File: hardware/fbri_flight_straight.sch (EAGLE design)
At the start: 38 parts, among them U1 SAM_D20E, U2 SI4060, U3 MAX1947, U4 ANTENOVA_GPS_M10382, U5 S25FS-S

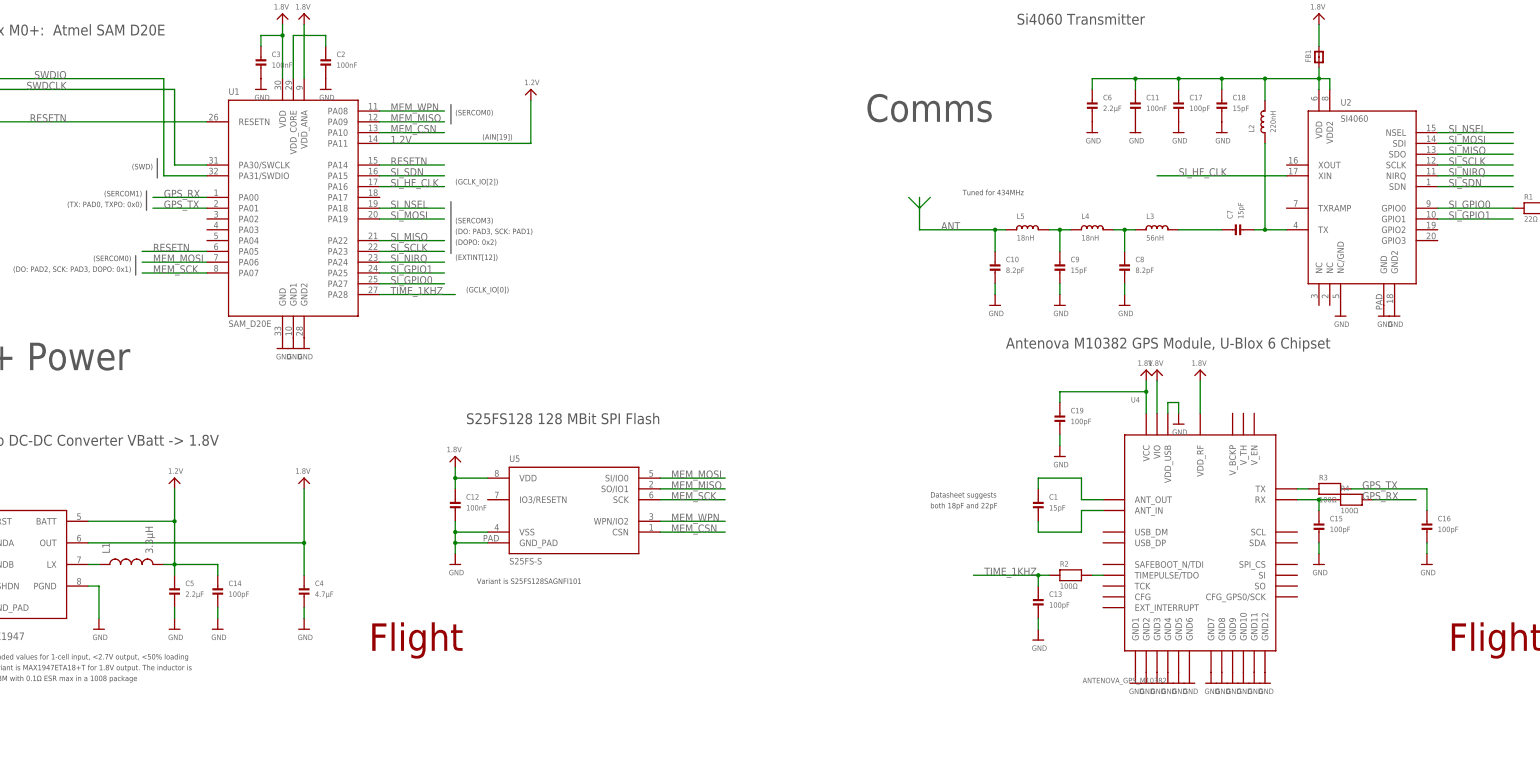
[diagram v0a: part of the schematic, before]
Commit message: Nearly there, about to re-work MAX1947
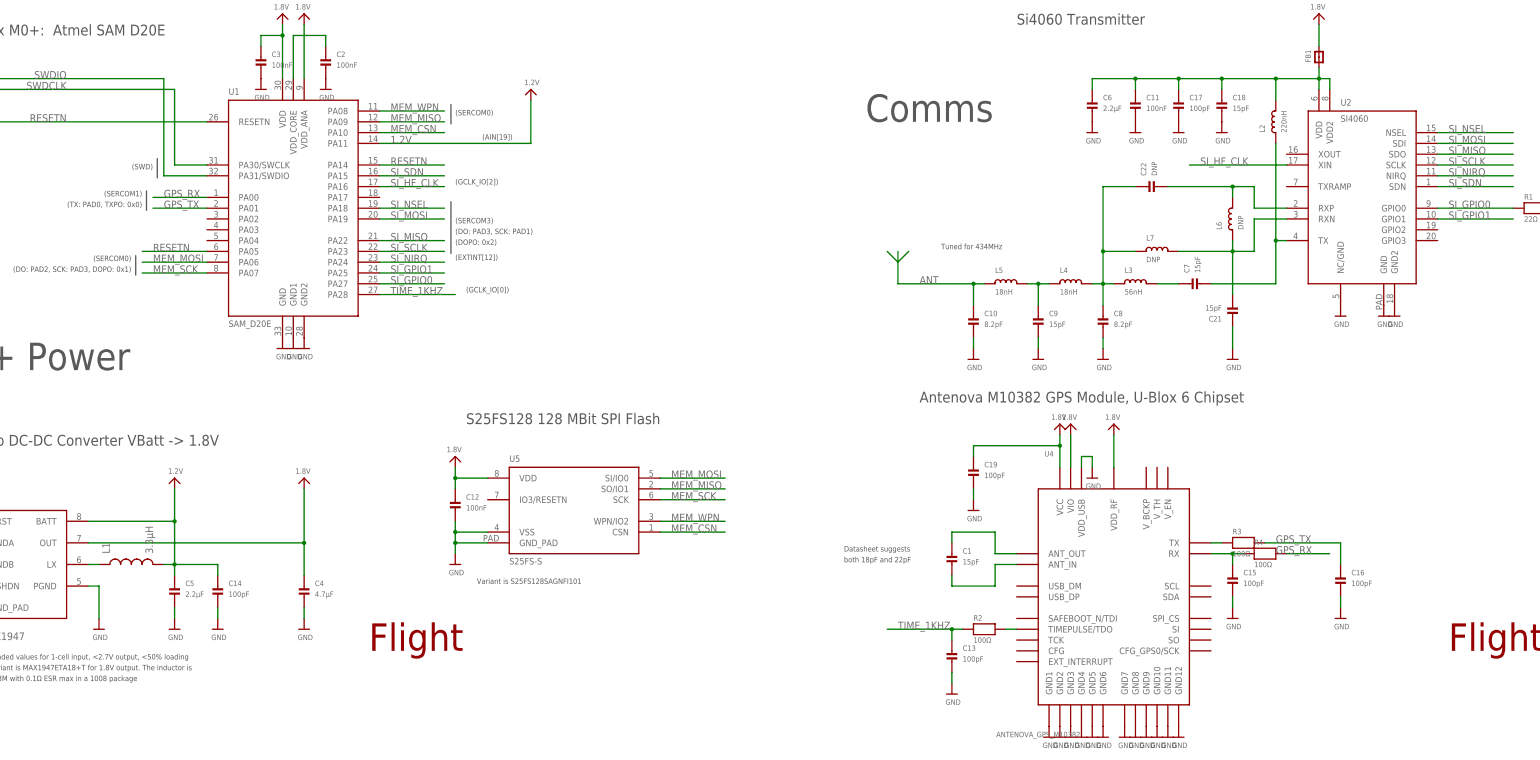
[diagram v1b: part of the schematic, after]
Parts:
- added C21: 15pF, microbuilder_v3:CAP_CERAMIC_0402
- added C22: DNP, microbuilder_v3:CAP_CERAMIC_0402
- added L6, L7: DNP, microbuilder_v3:INDUCTOR_0402
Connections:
- new net RXN: C21.P$2, L6.1, L7.2, U2.RXN
- new net RXP: C22.P$2, L6.2, U2.RXP
- net FILTER1: now also C22.P$1, L7.1
- net GND: now also C21.P$1
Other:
- moved on the sheet: C1, C10, C13, C15, C16, C19, C7, C8, C9, L2, L3, L4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

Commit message: Before rename
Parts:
- removed C4: 4.7µF, microbuilder_v3:CAP_CERAMIC_0402
- added C23: 4.7µF, resistor:C-EUC0603K
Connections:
- net 1.8V: now also C23.1; no longer C4.P$1
- net GND: now also C23.2; no longer C4.P$2
- net RESETN: now also U1.PA15; no longer U1.PA14
- net SI_HF_CLK: now also U1.PA17; no longer U1.PA16
- net SI_SDN: now also U1.PA16; no longer U1.PA15
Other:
- note added: "(GCLK_IO[3])"
- note removed: "(GCLK_IO[2])"
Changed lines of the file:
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@@
 <part name="U$1" library="microbuilder_v3" deviceset="GND" device=""/>
 <part name="U$28" library="microbuilder_v3" deviceset="GND" device=""/>
-<part name="C4" library="microbuilder_v3" deviceset="CAP_CERAMIC" device="_0402" value="4.7µF"/>
 <part name="U$29" library="microbuilder_v3" deviceset="GND" device=""/>
 <part name="U$30" library="microbuilder_v3" deviceset="1.8V" device=""/>
@@
 <part name="L7" library="microbuilder_v3" deviceset="INDUCTOR" device="_0402" value="DNP"/>
 <part name="C22" library="microbuilder_v3" deviceset="CAP_CERAMIC" device="_0402" value="DNP"/>
+<part name="C23" library="resistor" deviceset="C-EU" device="C0603K" value="4.7µF"/>
 </parts>
 <sheets>
@@
 <wire x1="169.164" y1="153.924" x2="169.164" y2="149.352" width="0.1524" layer="97"/>
 <text x="93.98" y="114.554" size="1.27" layer="97" font="vector" ratio="11" rot="MR0">(DO: PAD2, SCK: PAD3, DOPO: 0x1)</text>
-<text x="170.18" y="135.128" size="1.27" layer="97" font="vector" ratio="11">(GCLK_IO[2])</text>
+<text x="170.18" y="132.588" size="1.27" layer="97" font="vector" ratio="11">(GCLK_IO[3])</text>
 <text x="96.52" y="132.334" size="1.27" layer="97" font="vector" ratio="11" rot="MR0">(SERCOM1)</text>
 <wire x1="97.536" y1="133.604" x2="97.536" y2="129.032" width="0.1524" layer="97"/>
@@
 <instance part="U$1" gate="G$1" x="50.8" y="30.48"/>
 <instance part="U$28" gate="G$1" x="86.36" y="30.48"/>
-<instance part="C4" gate="G$1" x="134.62" y="38.1"/>
 <instance part="U$29" gate="G$1" x="134.62" y="30.48"/>
 <instance part="U$30" gate="G$1" x="134.62" y="66.04" rot="MR0"/>
@@
 <instance part="L7" gate="G$1" x="335.28" y="119.38"/>
 <instance part="C22" gate="G$1" x="335.28" y="134.62" rot="R90"/>
+<instance part="C23" gate="G$1" x="134.62" y="43.18"/>
 </instances>
 <busses>
@@
 <segment>
 <pinref part="U$29" gate="G$1" pin="GND"/>
-<pinref part="C4" gate="G$1" pin="P$2"/>
-<wire x1="134.62" y1="33.02" x2="134.62" y2="35.56" width="0.1524" layer="91"/>
+<pinref part="C23" gate="G$1" pin="2"/>
+<wire x1="134.62" y1="33.02" x2="134.62" y2="38.1" width="0.1524" layer="91"/>
 </segment>
 <segment>
@@
 </segment>
 <segment>
-<pinref part="U1" gate="G$1" pin="PA14"/>
-<wire x1="152.4" y1="139.7" x2="167.64" y2="139.7" width="0.1524" layer="91"/>
-<label x="154.94" y="139.7" size="1.778" layer="95" ratio="11"/>
+<pinref part="U1" gate="G$1" pin="PA15"/>
+<wire x1="152.4" y1="137.16" x2="167.64" y2="137.16" width="0.1524" layer="91"/>
+<label x="154.94" y="137.16" size="1.778" layer="95"/>
 </segment>
 </net>
@@
 <segment>
 <pinref part="U3" gate="G$1" pin="OUT"/>
-<pinref part="C4" gate="G$1" pin="P$1"/>
 <wire x1="83.82" y1="50.8" x2="134.62" y2="50.8" width="0.1524" layer="91"/>
-<wire x1="134.62" y1="50.8" x2="134.62" y2="43.18" width="0.1524" layer="91"/>
 <pinref part="U$30" gate="G$1" pin="1.8V"/>
 <wire x1="134.62" y1="50.8" x2="134.62" y2="63.5" width="0.1524" layer="91"/>
 <junction x="134.62" y="50.8"/>
+<pinref part="C23" gate="G$1" pin="1"/>
+<wire x1="134.62" y1="50.8" x2="134.62" y2="45.72" width="0.1524" layer="91"/>
 </segment>
 <segment>
@@
 </segment>
 <segment>
-<pinref part="U1" gate="G$1" pin="PA16"/>
-<wire x1="152.4" y1="134.62" x2="167.64" y2="134.62" width="0.1524" layer="91"/>
-<label x="154.94" y="134.62" size="1.778" layer="95" ratio="11"/>
+<pinref part="U1" gate="G$1" pin="PA17"/>
+<wire x1="152.4" y1="132.08" x2="167.64" y2="132.08" width="0.1524" layer="91"/>
+<label x="154.94" y="132.08" size="1.778" layer="95"/>
 </segment>
 </net>
 <net name="SI_SDN" class="0">
-<segment>
-<pinref part="U1" gate="G$1" pin="PA15"/>
-<wire x1="152.4" y1="137.16" x2="167.64" y2="137.16" width="0.1524" layer="91"/>
-<label x="154.94" y="137.16" size="1.778" layer="95" ratio="11"/>
-</segment>
 <segment>
 <pinref part="U2" gate="G$1" pin="SDN"/>
@@
 <label x="403.86" y="134.62" size="1.778" layer="95" ratio="11"/>
 </segment>
-</net>
+<segment>
+<pinref part="U1" gate="G$1" pin="PA16"/>
+<wire x1="152.4" y1="134.62" x2="167.64" y2="134.62" width="0.1524" layer="91"/>
+<label x="154.94" y="134.62" size="1.778" layer="95"/>
+</segment>
+</net>
